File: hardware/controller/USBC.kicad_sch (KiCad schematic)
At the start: 1 part, among them J1 USB_C_Receptacle_USB2.0_16P

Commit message: asdasd
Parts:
- J1: value USB_C_Receptacle_USB2.0_16P -> Joystick; footprint (none) -> Connector_USB:USB_C_Receptacle_GCT_USB4105-xx-A_16P_TopMnt_Horizontal
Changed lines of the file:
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@@
 			)
 		)
-		(property "Value" "USB_C_Receptacle_USB2.0_16P"
+		(property "Value" "Joystick"
 			(at 71.12 57.15 0)
 			(effects
@@
 			)
 		)
-		(property "Footprint" ""
+		(property "Footprint" "Connector_USB:USB_C_Receptacle_GCT_USB4105-xx-A_16P_TopMnt_Horizontal"
 			(at 74.93 77.47 0)
 			(effects
@@
 			)
 		)
-		(property "Datasheet" "https://www.usb.org/sites/default/files/documents/usb_type-c.zip"
+		(property "Datasheet" "https://www.sparkfun.com/products/9032"
 			(at 74.93 77.47 0)
 			(effects

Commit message: a
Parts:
- added D1, D2, D3: SMAJ5.0CA, Diode_SMD:Infineon_SG-WLL-2-3_0.58x0.28_P0.36mm, symbol Diode:ESD131-B1-W0201
- added D4: V2F22HM3_A_H, Diode_SMD:D_SMA, symbol Diode:SS3150
- added R25, R26: 5k1, symbol Device:R
- J1: value Joystick -> ~
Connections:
- net VBUS: now also J1.A4 (VBUS), J1.A9 (VBUS), J1.B4 (VBUS), J1.B9 (VBUS), D3.2 (A2), D4.1 (K), D4.2 (A)
- net GND: now reaches J1.A1 (GND), J1.A12 (GND), J1.B1 (GND), J1.B12 (GND)
- net GND: now also J1.S1 (SHIELD), D1.1 (A1), D2.1 (A1), D3.1 (A1), R25.2, R26.2
- net CC1: now reaches J1.A5 (CC1)
- net CC1: now also R25.1
- net USB+: now reaches J1.A6 (D+)
- net USB+: now also J1.B6 (D+), D2.2 (A2)
- net USB-: now reaches J1.A7 (D-)
- net USB-: now also J1.B7 (D-), D1.2 (A2)
- net CC2: now reaches J1.B5 (CC2)
- net CC2: now also R26.1
- no-connect marks 0 -> 2
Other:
- moved on the sheet: J1

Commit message: fixed bus stuff
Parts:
- renumbered R25 to R1, R26 to R2
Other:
- moved on the sheet: D3
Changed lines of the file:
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@@
+	(wire
+		(pts
+			(xy 172.72 73.66) (xy 172.72 69.85)
+		)
+		(stroke
+			(width 0)
+			(type default)
+		)
+	)
 	(wire
 		(pts
@@
 	(wire
 		(pts
-			(xy 172.72 77.47) (xy 172.72 99.06)
+			(xy 172.72 81.28) (xy 172.72 97.79)
 		)
 		(stroke
@@
 		(dnp no)
 		(fields_autoplaced yes)
-		(property "Reference" "#PWR040"
+		(property "Reference" "#PWR01"
 			(at 97.79 120.65 0)
 			(effects
@@
 			(project ""
 				(path "/869bea87-c885-4ead-826b-3f34ceacafad/26d17bc2-e2ae-44e6-8fc3-d458d6e51b4a"
-					(reference "#PWR040")
+					(reference "#PWR01")
 					(unit 1)
 				)
@@
 		(dnp no)
 		(fields_autoplaced yes)
-		(property "Reference" "#PWR041"
+		(property "Reference" "#PWR03"
 			(at 146.05 82.55 0)
 			(effects
@@
 			(project ""
 				(path "/869bea87-c885-4ead-826b-3f34ceacafad/26d17bc2-e2ae-44e6-8fc3-d458d6e51b4a"
-					(reference "#PWR041")
+					(reference "#PWR03")
 					(unit 1)
 				)
@@
 	(symbol
 		(lib_id "Diode:ESD131-B1-W0201")
-		(at 172.72 73.66 90)
+		(at 172.72 77.47 90)
 		(unit 1)
 		(exclude_from_sim no)
@@
 		(fields_autoplaced yes)
 		(property "Reference" "D3"
-			(at 175.26 72.3899 90)
+			(at 175.26 76.1999 90)
 			(effects
 				(font
@@
 		)
 		(property "Value" "SMAJ5.0CA"
-			(at 175.26 74.9299 90)
+			(at 175.26 78.7399 90)
 			(effects
 				(font
@@
 		)
 		(property "Footprint" "Diode_SMD:Infineon_SG-WLL-2-3_0.58x0.28_P0.36mm"
-			(at 172.72 73.66 0)
+			(at 172.72 77.47 0)
 			(effects
 				(font
@@
 		)
 		(property "Datasheet" "https://www.infineon.com/dgdl/Infineon-ESD131-B1-W0201-DataSheet-v02_00-EN.pdf?fileId=5546d4625cc9456a015ce94850964889"
-			(at 172.72 73.66 0)
+			(at 172.72 77.47 0)
 			(effects
 				(font
@@
 		)
 		(property "Description" "Bidirectional ESD protection diode, ±5.5Vrwm, 0.23pF, SG-WLL-2-3"
-			(at 172.72 73.66 0)
+			(at 172.72 77.47 0)
 			(effects
 				(font
@@
 		)
 		(property "Height" "2.29"
-			(at 566.37 60.96 0)
+			(at 566.37 64.77 0)
 			(effects
 				(font
@@
 		)
 		(property "Mouser Part Number" "576-SMAJ5.0CA"
-			(at 666.37 60.96 0)
+			(at 666.37 64.77 0)
 			(effects
 				(font
@@
 		)
 		(property "Mouser Price/Stock" "https://www.mouser.co.uk/ProductDetail/Littelfuse/SMAJ5.0CA?qs=JJML70Qc14u8hb22RFwTwA%3D%3D"
-			(at 766.37 60.96 0)
+			(at 766.37 64.77 0)
 			(effects
 				(font
@@
 		)
 		(property "Manufacturer_Name" "LITTELFUSE"
-			(at 866.37 60.96 0)
+			(at 866.37 64.77 0)
 			(effects
 				(font
@@
 		)
 		(property "Manufacturer_Part_Number" "SMAJ5.0CA"
-			(at 966.37 60.96 0)
+			(at 966.37 64.77 0)
 			(effects
 				(font
@@
 		(on_board yes)
 		(dnp no)
-		(property "Reference" "R25"
+		(property "Reference" "R1"
 			(at 127.508 72.898 90)
 			(effects
@@
 			(project ""
 				(path "/869bea87-c885-4ead-826b-3f34ceacafad/26d17bc2-e2ae-44e6-8fc3-d458d6e51b4a"
-					(reference "R25")
+					(reference "R1")
 					(unit 1)
 				)
@@
 		(dnp no)
 		(fields_autoplaced yes)
-		(property "Reference" "#PWR043"
+		(property "Reference" "#PWR04"
 			(at 158.75 104.14 0)
 			(effects
@@
 			(project "controller"
 				(path "/869bea87-c885-4ead-826b-3f34ceacafad/26d17bc2-e2ae-44e6-8fc3-d458d6e51b4a"
-					(reference "#PWR043")
+					(reference "#PWR04")
 					(unit 1)
 				)
@@
 	(symbol
 		(lib_id "power:GND")
-		(at 172.72 99.06 0)
+		(at 172.72 97.79 0)
 		(unit 1)
 		(exclude_from_sim no)
@@
 		(dnp no)
 		(fields_autoplaced yes)
-		(property "Reference" "#PWR044"
-			(at 172.72 105.41 0)
+		(property "Reference" "#PWR05"
+			(at 172.72 104.14 0)
 			(effects
 				(font
@@
 		)
 		(property "Value" "GND"
-			(at 172.72 104.14 0)
+			(at 172.72 102.87 0)
 			(effects
 				(font
@@
 		)
 		(property "Footprint" ""
-			(at 172.72 99.06 0)
+			(at 172.72 97.79 0)
 			(effects
 				(font
@@
 		)
 		(property "Datasheet" ""
-			(at 172.72 99.06 0)
+			(at 172.72 97.79 0)
 			(effects
 				(font
@@
 		)
 		(property "Description" "Power symbol creates a global label with name \"GND\" , ground"
-			(at 172.72 99.06 0)
+			(at 172.72 97.79 0)
 			(effects
 				(font
@@
 			(project ""
 				(path "/869bea87-c885-4ead-826b-3f34ceacafad/26d17bc2-e2ae-44e6-8fc3-d458d6e51b4a"
-					(reference "#PWR044")
+					(reference "#PWR05")
 					(unit 1)
 				)
@@
 		(on_board yes)
 		(dnp no)
-		(property "Reference" "R26"
+		(property "Reference" "R2"
 			(at 136.398 76.708 90)
 			(effects
@@
 			(project "controller"
 				(path "/869bea87-c885-4ead-826b-3f34ceacafad/26d17bc2-e2ae-44e6-8fc3-d458d6e51b4a"
-					(reference "R26")
+					(reference "R2")
 					(unit 1)
 				)
@@
 		(dnp no)
 		(fields_autoplaced yes)
-		(property "Reference" "#PWR042"
+		(property "Reference" "#PWR02"
 			(at 143.51 104.14 0)
 			(effects
@@
 			(project "controller"
 				(path "/869bea87-c885-4ead-826b-3f34ceacafad/26d17bc2-e2ae-44e6-8fc3-d458d6e51b4a"
-					(reference "#PWR042")
+					(reference "#PWR02")
 					(unit 1)
 				)

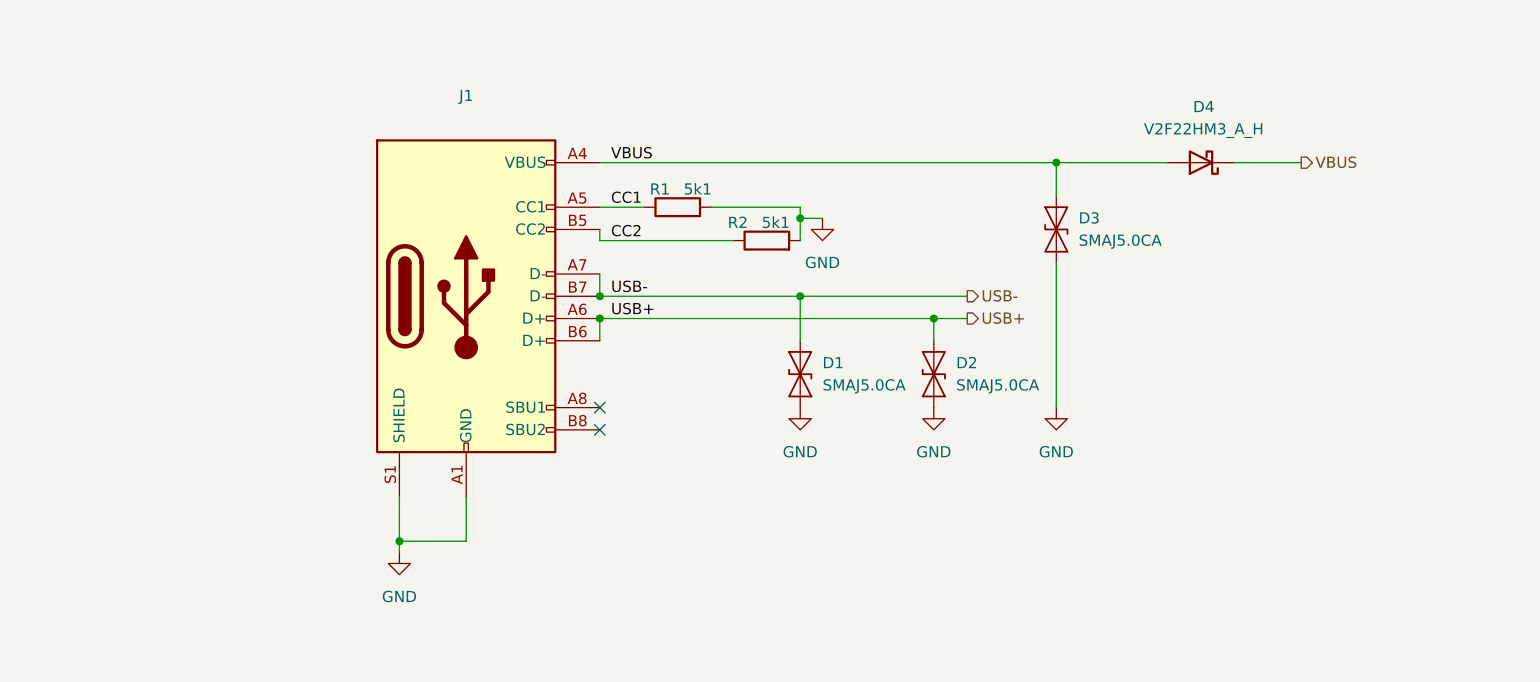
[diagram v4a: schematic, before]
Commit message: modified power circuitry
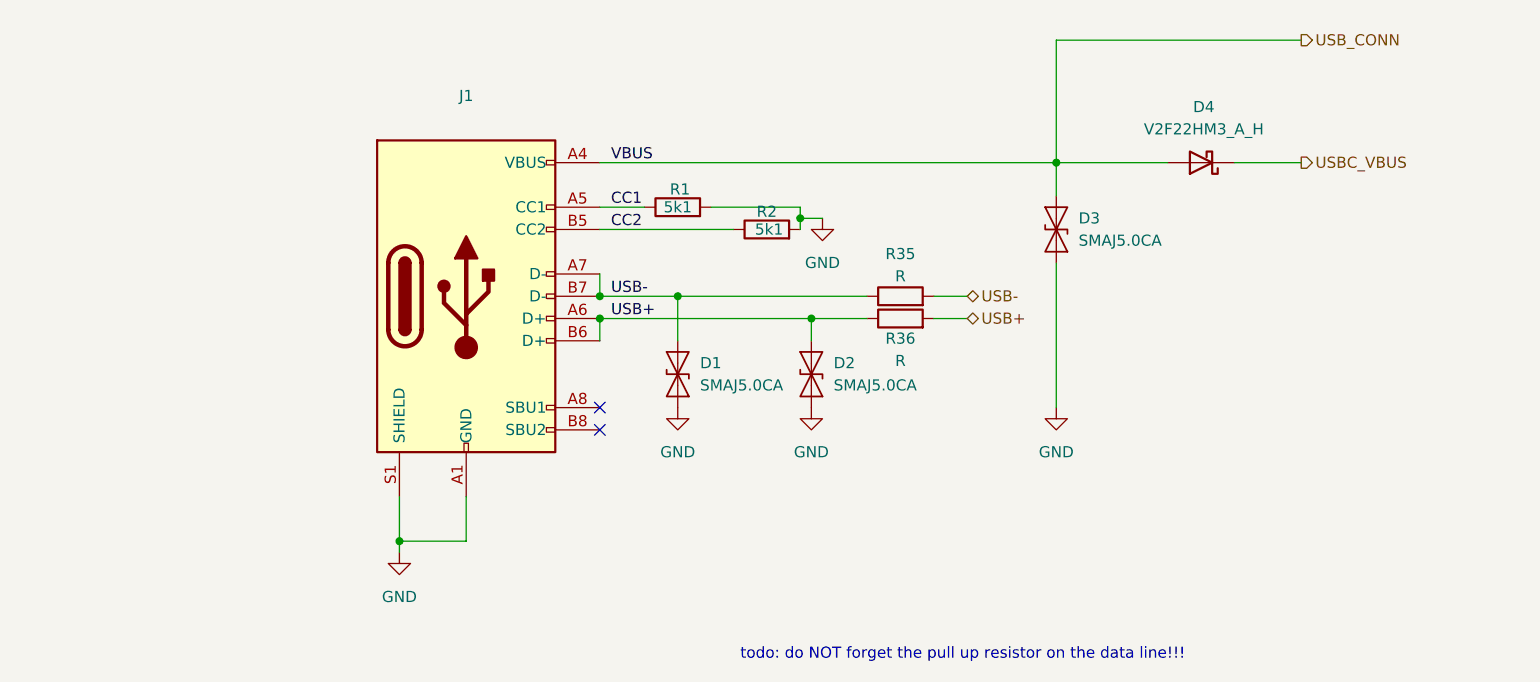
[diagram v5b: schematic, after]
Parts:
- added R35, R36: R, symbol Device:R
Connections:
- net USB+: now also R36.1, R36.2
- net USB-: now also R35.1, R35.2
- net VBUS renamed USB_CONN
- net USB_CONN: no longer D4.1 (K)
- new net USBC_VBUS: D4.1 (K)
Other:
- note added: "todo: do NOT forget the pull up resistor on the data line!!!"
- moved on the sheet: D1, D2, R2

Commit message: finished first rev of controller schematic minus actually finding passive components. moved some features to rev2 todo
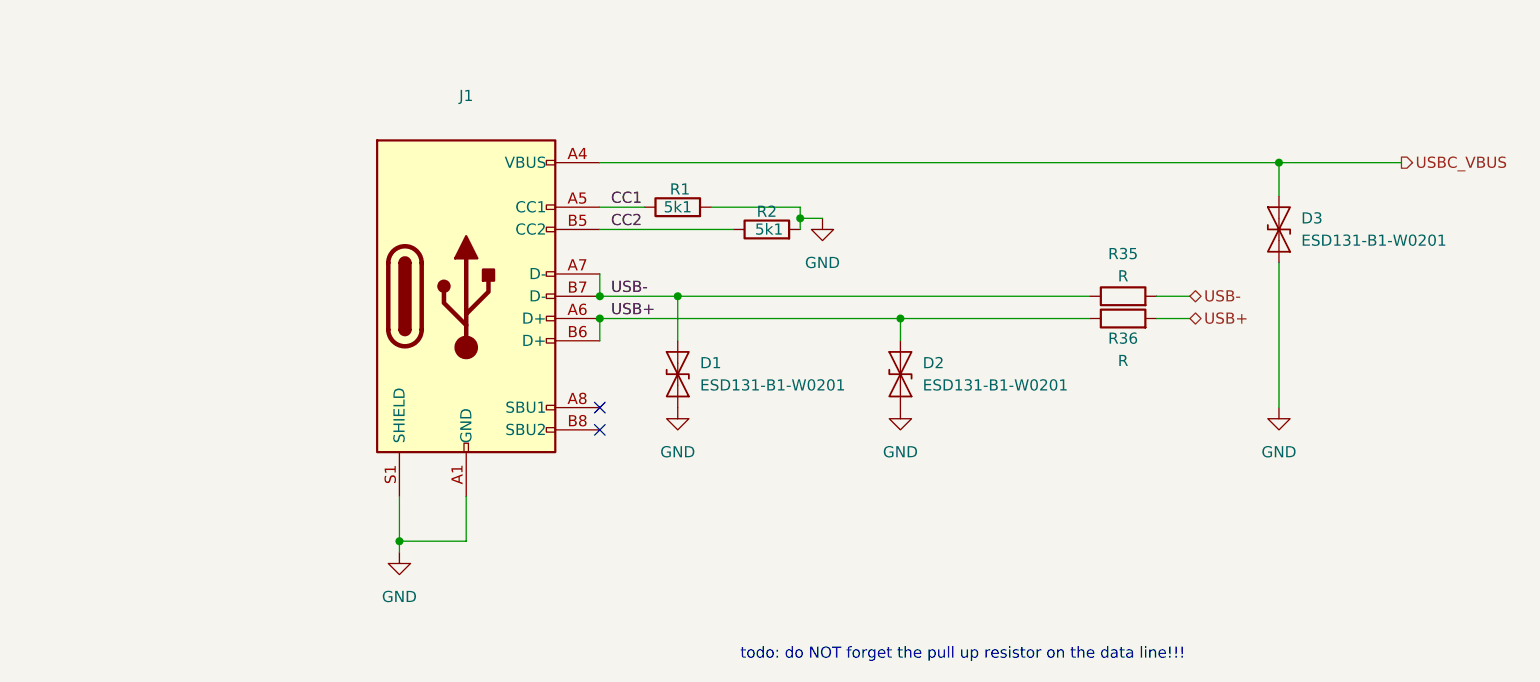
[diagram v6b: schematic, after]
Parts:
- removed D4: V2F22HM3_A_H, Diode_SMD:D_SMA, symbol Diode:SS3150
- D1, D2, D3: value SMAJ5.0CA -> ESD131-B1-W0201
- J1: footprint Connector_USB:USB_C_Receptacle_GCT_USB4105-xx-A_16P_TopMnt_Horizontal -> SamacSys_Parts:USB_C_Receptacle_GCT_USB4105-xx-A_16P_TopMnt_Horizontal
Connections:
- net USB_CONN is gone; now on net USBC_VBUS: D3.2 (A2), J1.A4 (VBUS), J1.A9 (VBUS), J1.B4 (VBUS), J1.B9 (VBUS)
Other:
- moved on the sheet: D2, D3, R35, R36

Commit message: Moved LEDs around. Replaced some discrete resistors with resistor arrays. Added mounting holes. Added. Added a lot of actual components for passive elements
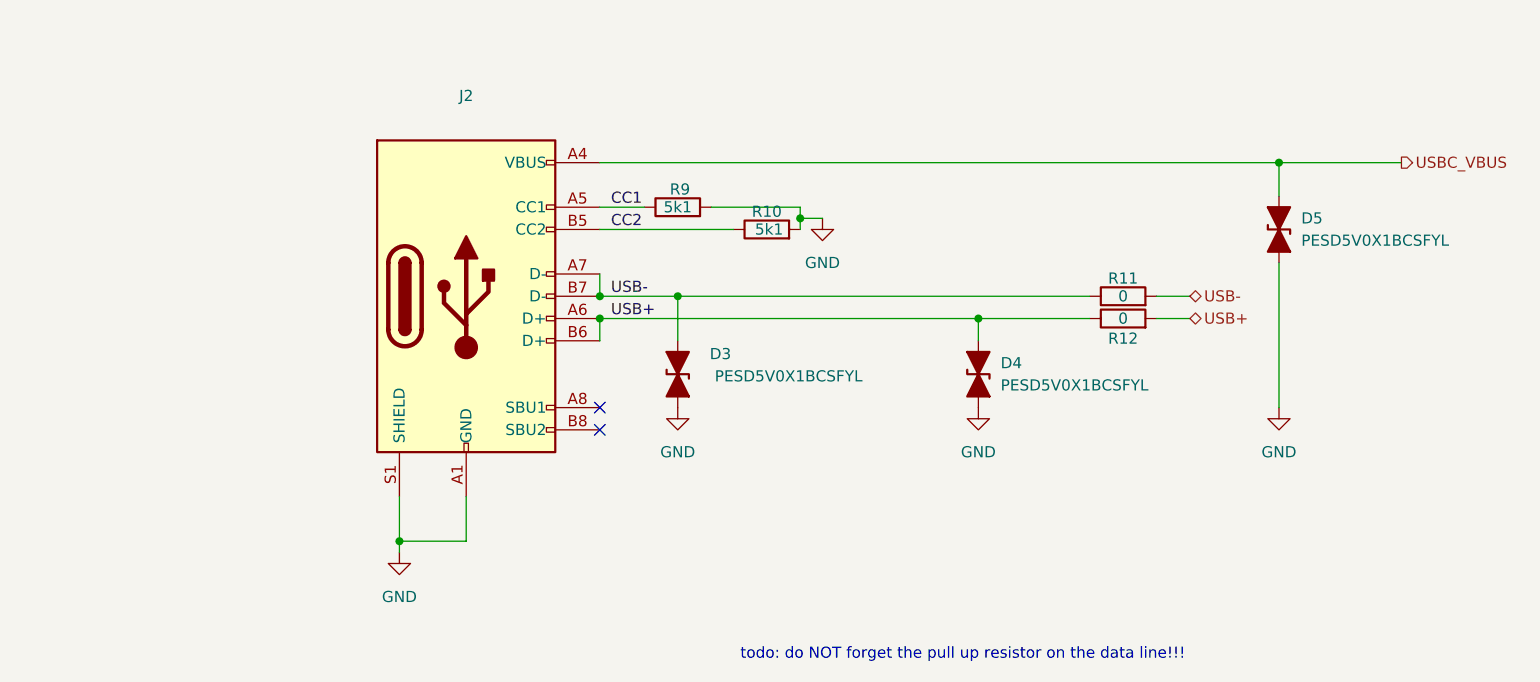
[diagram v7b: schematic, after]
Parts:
- D3: renamed from D1; value ESD131-B1-W0201 -> PESD5V0X1BCSFYL; footprint Diode_SMD:Infineon_SG-WLL-2-3_0.58x0.28_P0.36mm -> PMEG3005AESFYL; symbol Diode:ESD131-B1-W0201 -> Device:D_TVS_Filled; Height 2.29 -> 0.16; Manufacturer_Name LITTELFUSE -> Nexperia; Manufacturer_Part_Number SMAJ5.0CA -> PESD5V0X1BCSFYL; Mouser Part Number 576-SMAJ5.0CA -> 771-PESD5V0X1BCSFYL; Mouser Price/Stock https://www.mouser.co.uk/ProductDetail/Littelfuse/SMAJ5.0CA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 -> https://www.mouser.co.uk/ProductDetail/Nexperia/PESD5V0X1BC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
- D4: renamed from D2; value ESD131-B1-W0201 -> PESD5V0X1BCSFYL; footprint Diode_SMD:Infineon_SG-WLL-2-3_0.58x0.28_P0.36mm -> PMEG3005AESFYL; symbol Diode:ESD131-B1-W0201 -> Device:D_TVS_Filled; Height 2.29 -> 0.16; Manufacturer_Name LITTELFUSE -> Nexperia; Manufacturer_Part_Number SMAJ5.0CA -> PESD5V0X1BCSFYL; Mouser Part Number 576-SMAJ5.0CA -> 771-PESD5V0X1BCSFYL; Mouser Price/Stock https://www.mouser.co.uk/ProductDetail/Littelfuse/SMAJ5.0CA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 -> https://www.mouser.co.uk/ProductDetail/Nexperia/PESD5V0X1BC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
- D5: renamed from D3; value ESD131-B1-W0201 -> PESD5V0X1BCSFYL; footprint Diode_SMD:Infineon_SG-WLL-2-3_0.58x0.28_P0.36mm -> PMEG3005AESFYL; symbol Diode:ESD131-B1-W0201 -> Device:D_TVS_Filled; Height 2.29 -> 0.16; Manufacturer_Name LITTELFUSE -> Nexperia; Manufacturer_Part_Number SMAJ5.0CA -> PESD5V0X1BCSFYL; Mouser Part Number 576-SMAJ5.0CA -> 771-PESD5V0X1BCSFYL; Mouser Price/Stock https://www.mouser.co.uk/ProductDetail/Littelfuse/SMAJ5.0CA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 -> https://www.mouser.co.uk/ProductDetail/Nexperia/PESD5V0X1BC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
- R11: renamed from R35; value R -> 0; footprint (none) -> RESC1608X50N; Height (none) -> 0.5; Manufacturer_Name (none) -> Vishay; Manufacturer_Part_Number (none) -> CRCW06030000Z0EA; Mouser Part Number (none) -> 71-CRCW0603-0-E3; Mouser Price/Stock (none) -> https://www.mouser.co.uk/ProductDetail/Vishay-Dale/CRCW0603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
- R12: renamed from R36; value R -> 0; footprint (none) -> RESC1608X50N; Height (none) -> 0.5; Manufacturer_Name (none) -> Vishay; Manufacturer_Part_Number (none) -> CRCW06030000Z0EA; Mouser Part Number (none) -> 71-CRCW0603-0-E3; Mouser Price/Stock (none) -> https://www.mouser.co.uk/ProductDetail/Vishay-Dale/CRCW0603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
- renumbered J1 to J2, R2 to R10, R1 to R9

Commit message: ERC good to go. grouped all components on pcb
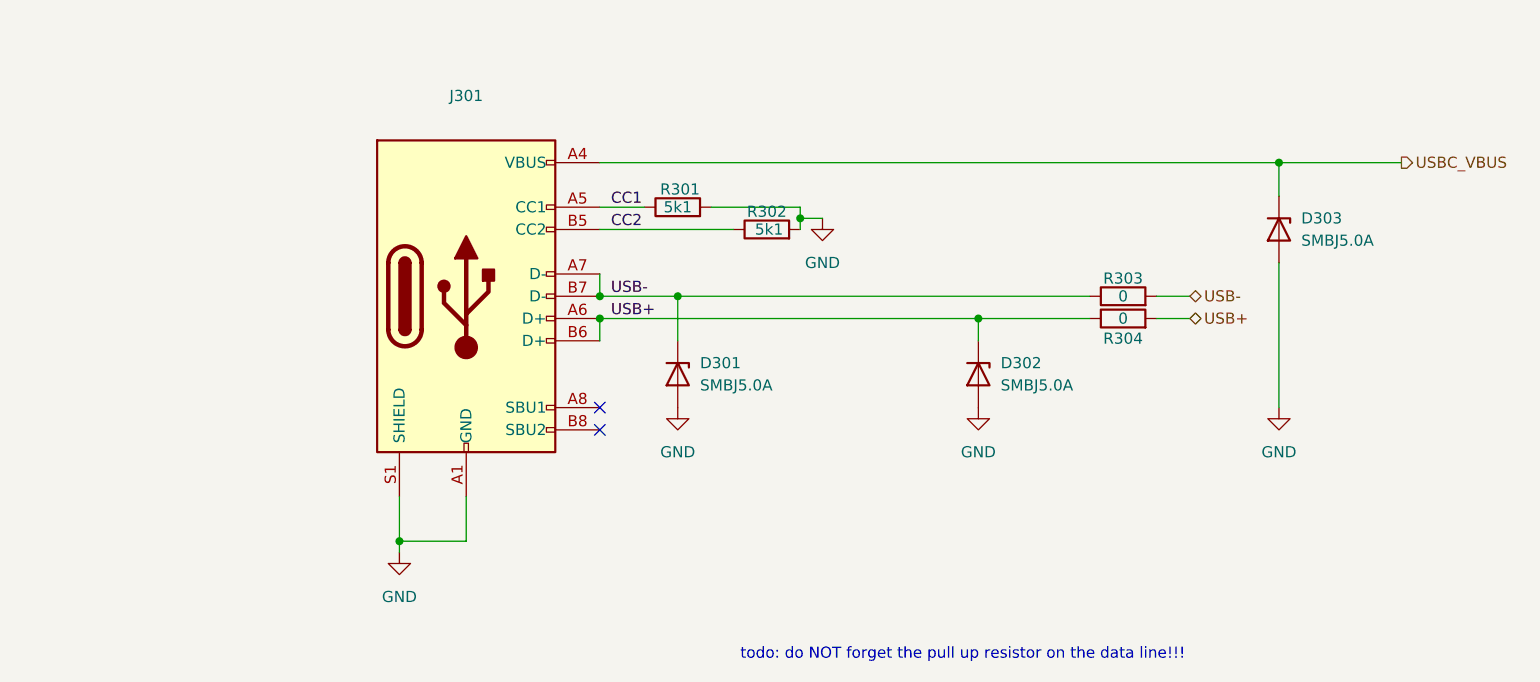
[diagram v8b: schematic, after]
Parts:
- removed D3, D4, D5: PESD5V0X1BCSFYL, PMEG3005AESFYL, symbol Device:D_TVS_Filled
- added D301, D302, D303: SMBJ5.0A, SamacSys_Parts:DIOM5436X261N, symbol Device:D_Zener
- R301: renamed from R9; footprint (none) -> SamacSys_Parts:RESC1608X50N; Height (none) -> 0.5; Manufacturer_Name (none) -> Vishay; Manufacturer_Part_Number (none) -> CRCW06035K10FKEC; Mouser Part Number (none) -> 71-CRCW06035K10FKEC; Mouser Price/Stock (none) -> https://www.mouser.co.uk/ProductDetail/Vishay-Dale/CRCW0603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
- R302: renamed from R10; footprint (none) -> SamacSys_Parts:RESC1608X50N; Height (none) -> 0.5; Manufacturer_Name (none) -> Vishay; Manufacturer_Part_Number (none) -> CRCW06035K10FKEC; Mouser Part Number (none) -> 71-CRCW06035K10FKEC; Mouser Price/Stock (none) -> https://www.mouser.co.uk/ProductDetail/Vishay-Dale/CRCW0603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
- R303: renamed from R11; footprint RESC1608X50N -> SamacSys_Parts:RESC1608X50N
- R304: renamed from R12; footprint RESC1608X50N -> SamacSys_Parts:RESC1608X50N
- renumbered J2 to J301
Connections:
- net GND: now also D301.2 (A), D302.2 (A), D303.2 (A)
- net USB+: now also D302.1 (K)
- net USB-: now also D301.1 (K)
- net USBC_VBUS: now also D303.1 (K)
